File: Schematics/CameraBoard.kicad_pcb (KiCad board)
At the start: 4 copper layers, 50 x 100 mm, 74 parts, among them J1 Microsemi_FlashPro-JTAG-10, J3 USB_C_Receptacle_USB2.0_16P, U1 STM32F405RGT6, U2 LDL1117-3.3, U3 TPS22917DBVR, U4 SN65HVD230, U5 TPS22917DBVR, U6 TPS22917DBVR, Y1 8mhz

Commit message: output files completed quote obtained
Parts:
- moved G*** 1.17 mm to (78.4, 52.7)

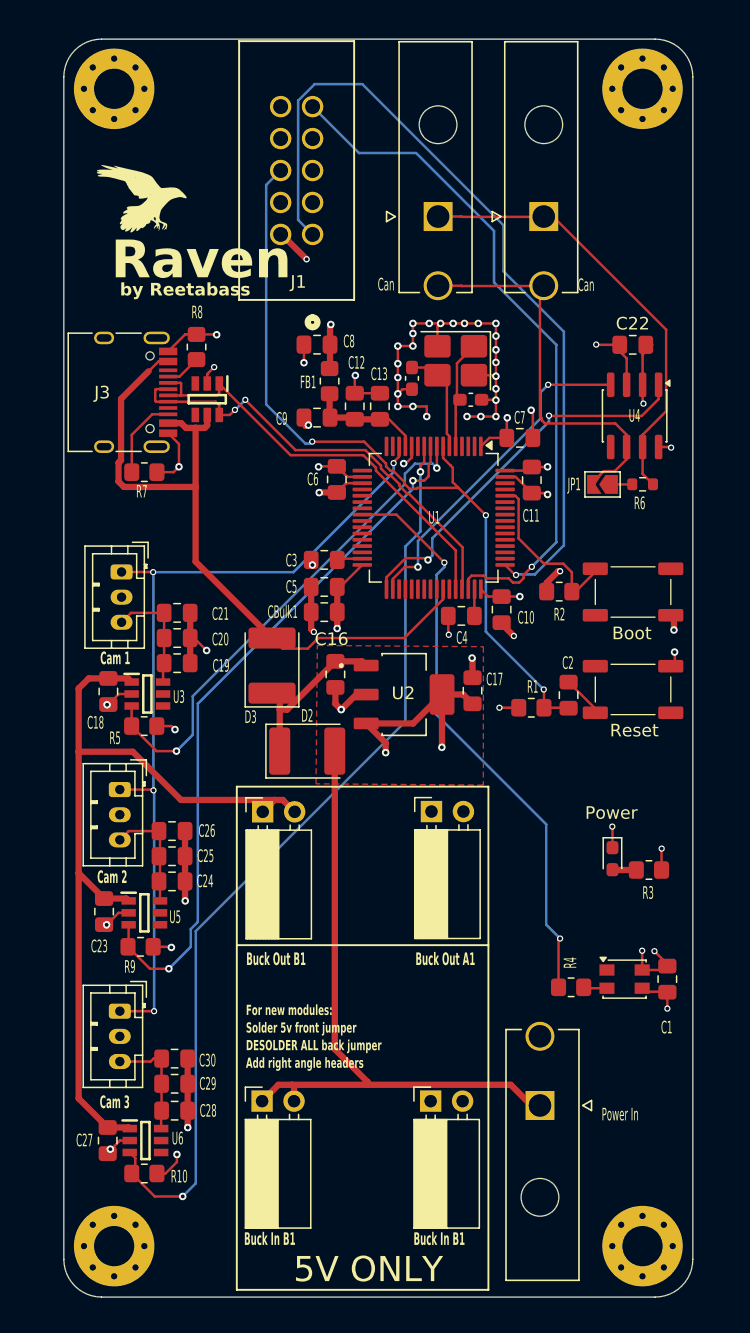
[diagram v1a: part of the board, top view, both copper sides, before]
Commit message: fixed buck converter routing
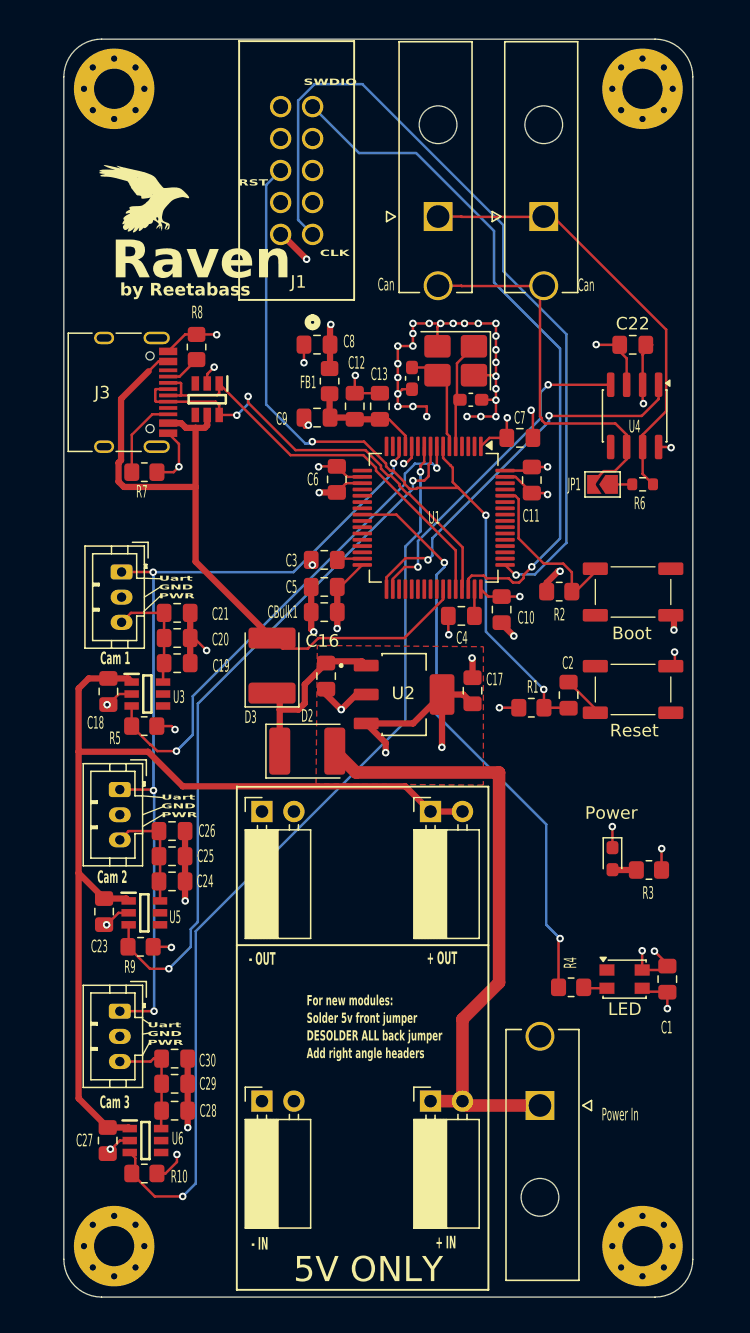
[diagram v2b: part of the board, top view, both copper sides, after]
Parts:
- moved J_BUCK_OUT_A1 13.5 mm to (87.2, 101.0)
- moved J_BUCK_IN_A1 13.4 mm to (87.2, 124.0)
- moved J_BUCK_IN_B1 13.4 mm to (100.6, 124.0)
- moved J_BUCK_OUT_B1 13.3 mm to (100.6, 101.0)
- moved C16 0.75 mm to (92.3, 90.2)
- moved G*** 0.20 mm to (78.6, 52.7)
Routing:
- net +5V: track 67.7 -> 79.7 mm
- net +BATT: track 52.5 -> 49.9 mm
- net /MCU/D+: track 36.0 -> 36.9 mm
- net Net-(D2-K): track 13.5 -> 14.3 mm
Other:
- board text added: "+ IN"
- board text added: "+ OUT"
- board text added: "- IN"
- board text added: "- OUT"
- board text added: "CLK"
- board text added: "GND"
- board text added: "LED"
- board text added: "PWR"
- board text added: "RST"
- board text added: "SWDIO"
- board text added: "Uart"
- board text removed: "Buck In B1"
- board text removed: "Buck Out A1"
- board text removed: "Buck Out B1"

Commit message: final output files
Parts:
- removed CBulk1: 4.7uf, Capacitor_SMD:C_0805_2012Metric_Pad1.18x1.45mm_HandSolder
- added C31: 4.7u, Capacitor_SMD:C_0805_2012Metric_Pad1.18x1.45mm_HandSolder, F.Cu at (92.1, 85.2)
- moved G*** 1.64 mm to (77.3, 51.7)
- moved J1 0.12 mm to (91.2, 55.2)
- moved CAN_IN1 0.09 mm to (109.6, 53.8)
- moved CAN_OUT1 0.09 mm to (101.2, 53.8)
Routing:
- net +5V: track 79.7 -> 80.8 mm
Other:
- board text removed: "SWDIO"

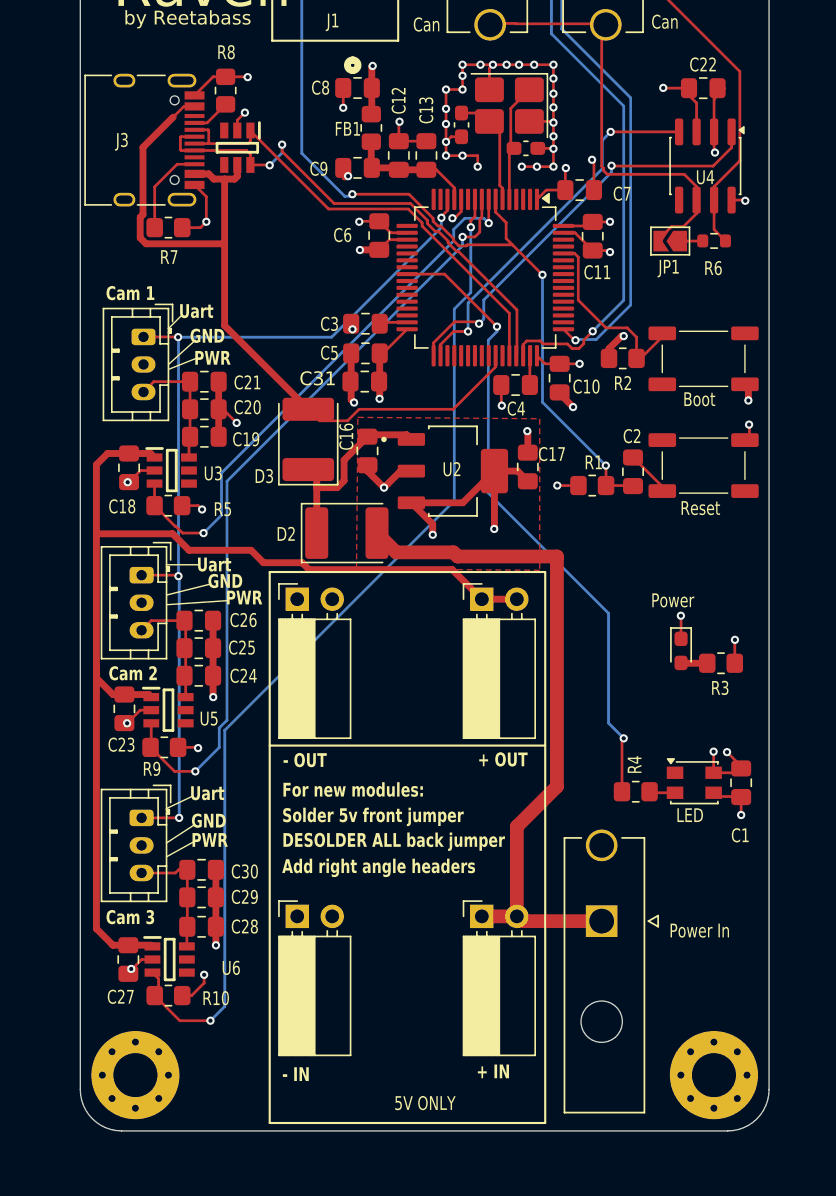
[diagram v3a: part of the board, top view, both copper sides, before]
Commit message: dfm complete sent for order
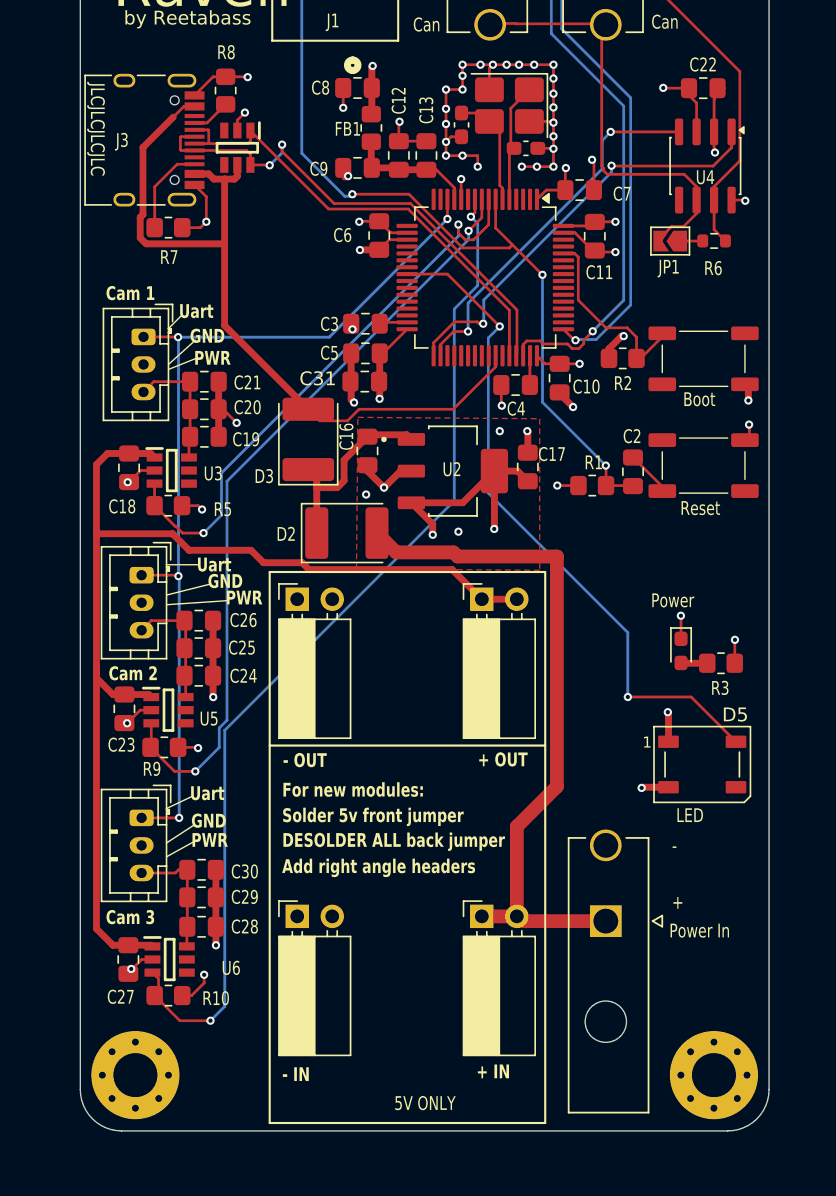
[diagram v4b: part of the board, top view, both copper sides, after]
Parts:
- removed C1: 100nf, Capacitor_SMD:C_0805_2012Metric_Pad1.18x1.45mm_HandSolder
- removed D1: NeoPixel_THT, LED_SMD:LED_Kingbright_AAA3528ESGCT
- removed R4: 330r, Resistor_SMD:R_0805_2012Metric_Pad1.20x1.40mm_HandSolder
- added D5: ws2812b, LED_SMD:LED_WS2812B_PLCC4_5.0x5.0mm_P3.2mm, F.Cu at (116.6, 113.0)
- moved PowerIn1 0.30 mm to (109.6, 124.4)
- moved C11 0.15 mm to (108.8, 74.7)
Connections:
- net /Camera_center/CAM_UART_TX renamed /Camera_center/CAM_UART_RX
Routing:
- net GND: track 113.8 -> 111.0 mm, vias 54 -> 56
- net /MCU/RGB_DATA: track 46.2 -> 48.9 mm
- net Net-(D1-DIN): track 1.78 -> 0.00 mm
- net /Camera_left/PWN_EN: track 39.9 -> 41.0 mm
- net /Camera_right/PWN_EN: track 56.5 -> 55.8 mm
- net +3.3V: track 61.1 -> 60.6 mm
- added copper zone on F.Cu, net GND
- removed copper zone on F.Cu, net +3.3V
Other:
- board text added: "+"
- board text added: "-"
- board text added: "JLCJLCJLCJLC"

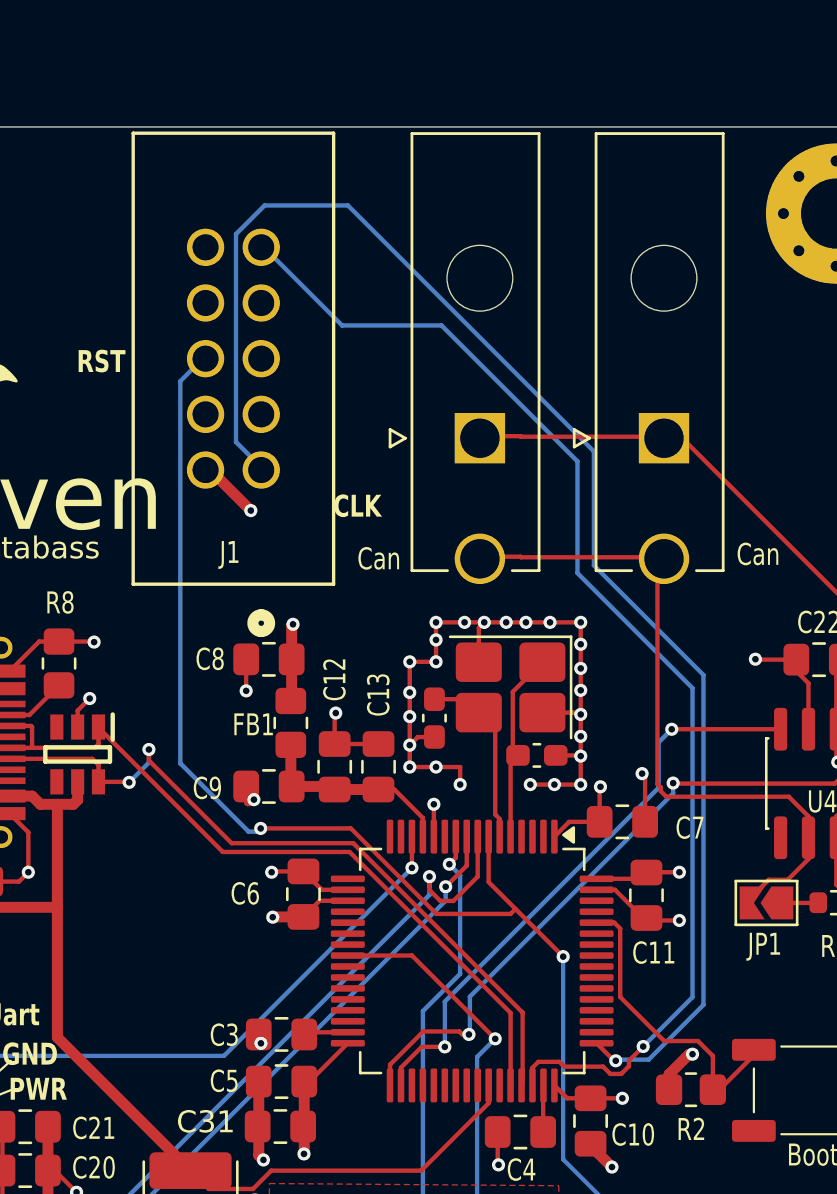
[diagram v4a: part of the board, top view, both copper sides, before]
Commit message: fixed can tranciver issues and updated to KiCad 10.0
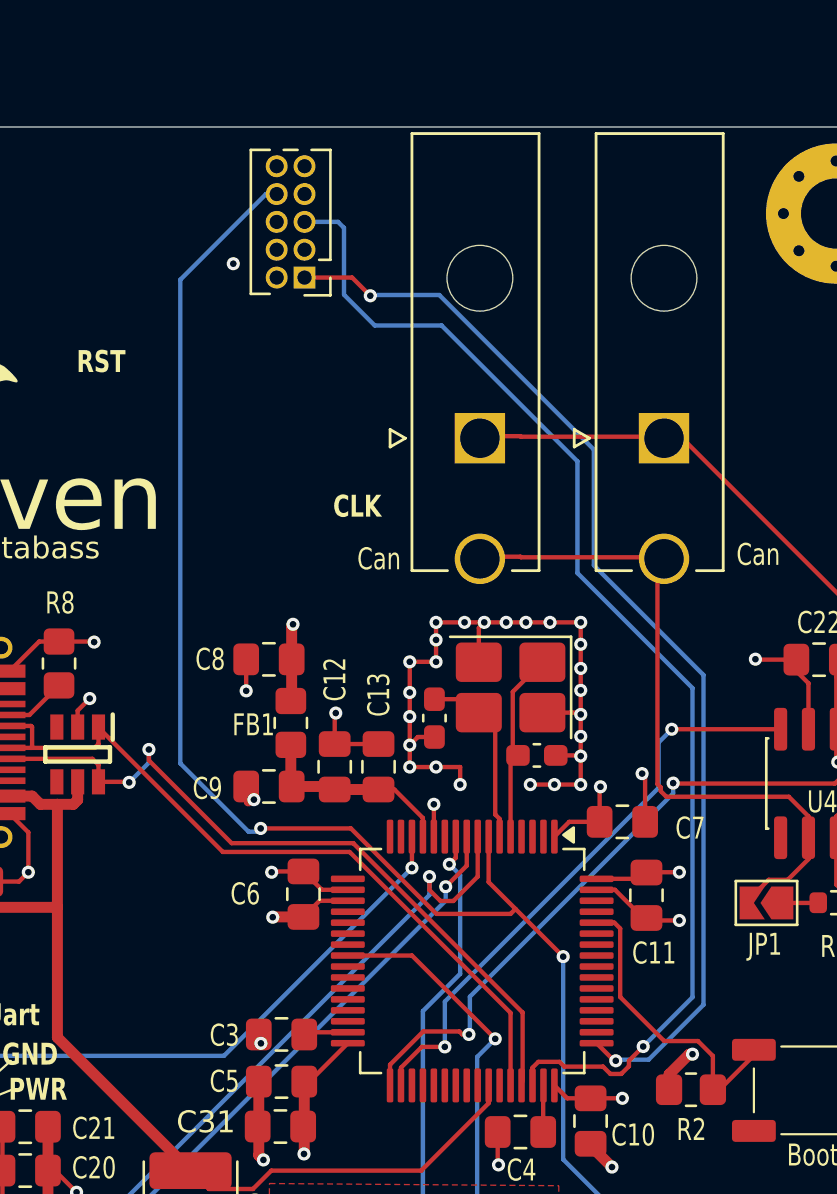
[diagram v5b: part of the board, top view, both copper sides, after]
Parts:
- J1: footprint myFootprints:CONN_7024610XX_MOL -> Connector_PinHeader_1.27mm:PinHeader_2x05_P1.27mm_Vertical
- moved J1 9.00 mm to (93.2, 46.5), turned to 180 degrees
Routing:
- net /MCU/SWCLK: track 66.2 -> 50.1 mm, vias 1 -> 2
- net /MCU/NRST: track 63.4 -> 72.5 mm

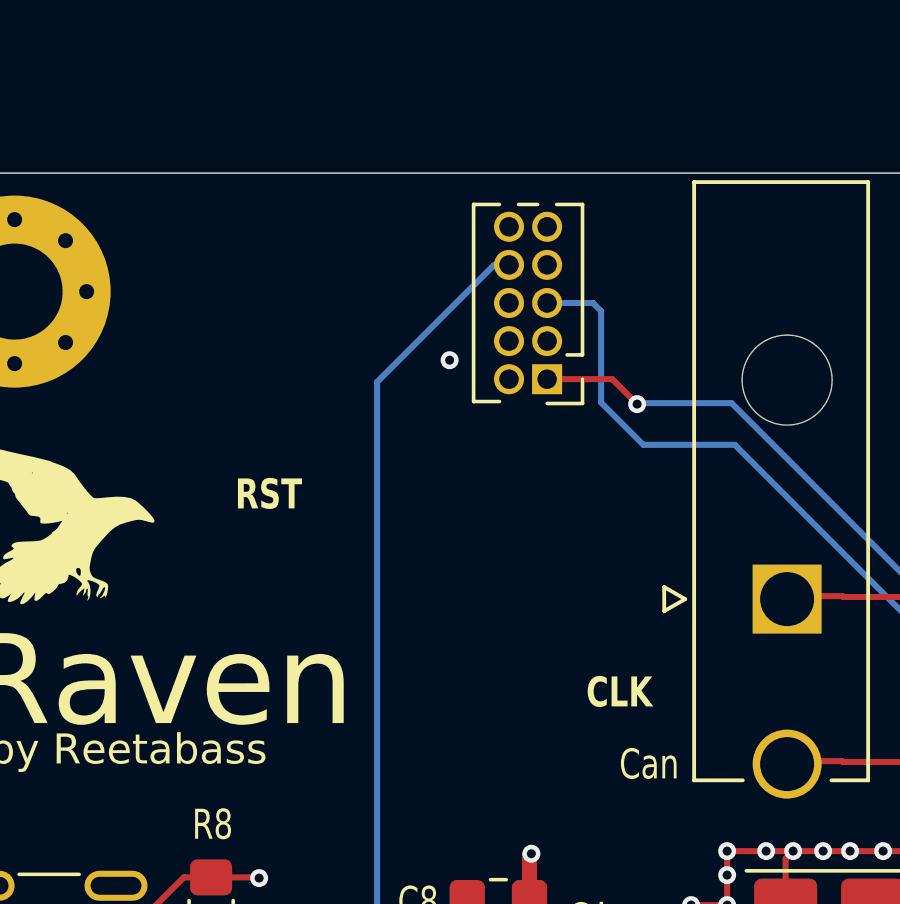
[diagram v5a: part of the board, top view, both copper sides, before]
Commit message: updated stlink connector
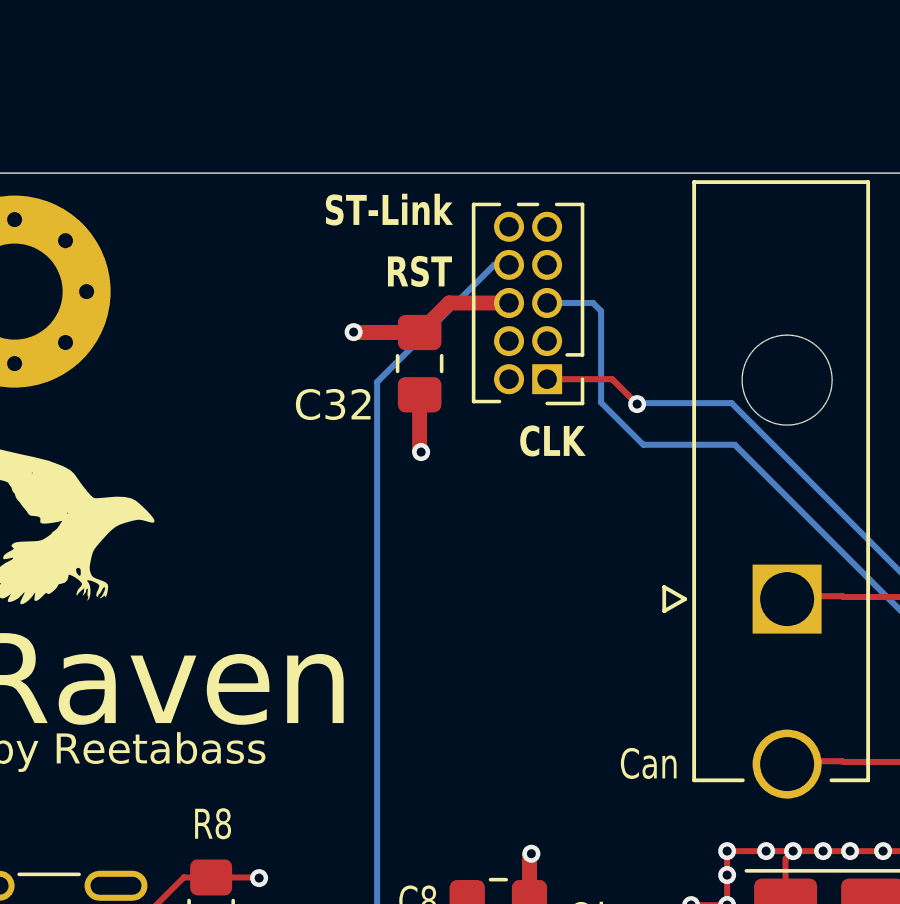
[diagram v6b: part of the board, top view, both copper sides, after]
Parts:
- added C32: 100nf, Capacitor_SMD:C_0805_2012Metric_Pad1.18x1.45mm_HandSolder, F.Cu at (89.0, 46.0)
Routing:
- net +3.3V: track 60.7 -> 63.5 mm
- net GND: track 111.0 -> 112.9 mm, vias 56 -> 57
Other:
- board text added: "ST-Link"
